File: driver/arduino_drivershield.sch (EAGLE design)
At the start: 13 parts, among them IC1 LB1973M, IC10 74HC14D, IC11 74HC14D, IC2 LB1973M, IC3 LB1973M, IC4 LB1973M, IC5 LB1973M, IC6 LB1973M, IC7 LB1973M, IC8 LB1973M, IC9 74HC14D, U1 ARDUINO_SHIELDLABEL

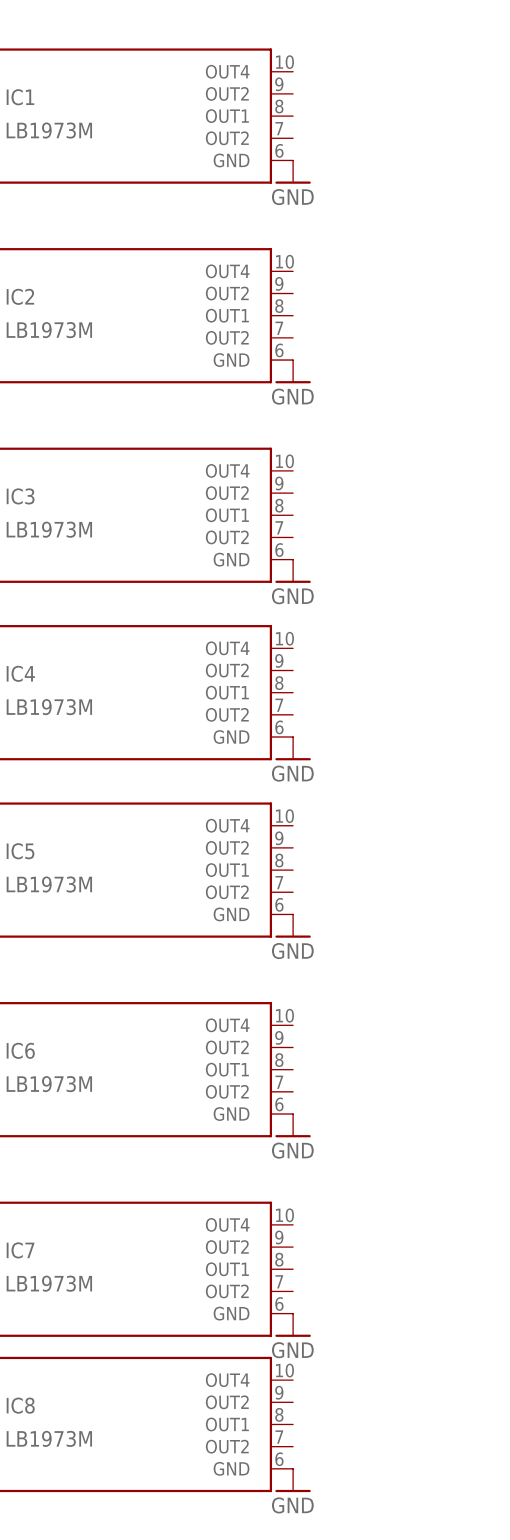
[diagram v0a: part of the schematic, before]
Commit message: 2x4 connectors for the coils
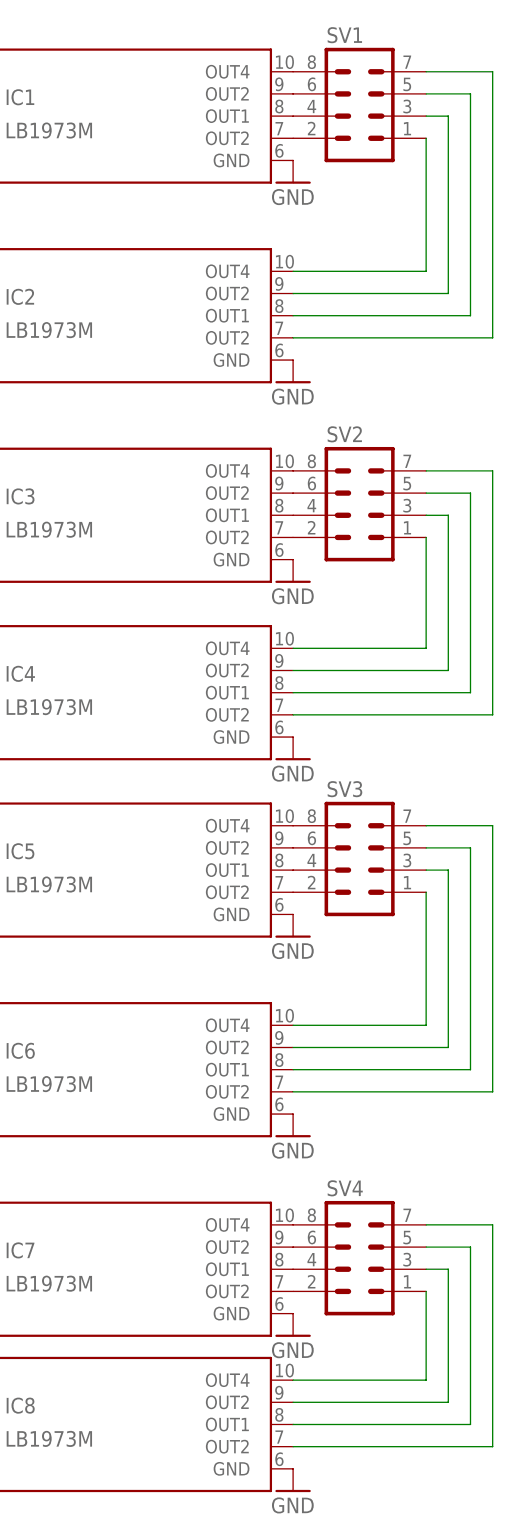
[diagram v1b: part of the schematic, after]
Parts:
- added SV1, SV2, SV3, SV4: (no value), con-lstb:MA04-2
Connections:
- new net N$33: IC1.OUT2, SV1.2
- new net N$34: IC1.OUT1, SV1.4
- new net N$35: IC1.OUT2@1, SV1.6
- new net N$36: IC1.OUT4, SV1.8
- new net N$37: IC3.OUT2, SV2.2
- new net N$38: IC3.OUT1, SV2.4
- new net N$39: IC3.OUT2@1, SV2.6
- new net N$40: IC3.OUT4, SV2.8
- new net N$41: IC5.OUT2, SV3.2
- new net N$42: IC5.OUT1, SV3.4
- new net N$43: IC5.OUT2@1, SV3.6
- new net N$44: IC5.OUT4, SV3.8
- new net N$45: IC7.OUT2, SV4.2
- new net N$46: IC7.OUT1, SV4.4
- new net N$47: IC7.OUT2@1, SV4.6
- new net N$48: IC7.OUT4, SV4.8
- new net N$49: IC8.OUT4, SV4.1
- new net N$50: IC8.OUT2@1, SV4.3
- new net N$51: IC8.OUT1, SV4.5
- new net N$52: IC8.OUT2, SV4.7
- new net N$53: IC6.OUT4, SV3.1
- new net N$54: IC6.OUT2@1, SV3.3
- new net N$55: IC6.OUT1, SV3.5
- new net N$56: IC6.OUT2, SV3.7
- new net N$57: IC4.OUT4, SV2.1
- new net N$58: IC4.OUT2@1, SV2.3
- new net N$59: IC4.OUT1, SV2.5
- new net N$60: IC4.OUT2, SV2.7
- new net N$61: IC2.OUT4, SV1.1
- new net N$62: IC2.OUT2@1, SV1.3
- new net N$63: IC2.OUT1, SV1.5
- new net N$64: IC2.OUT2, SV1.7

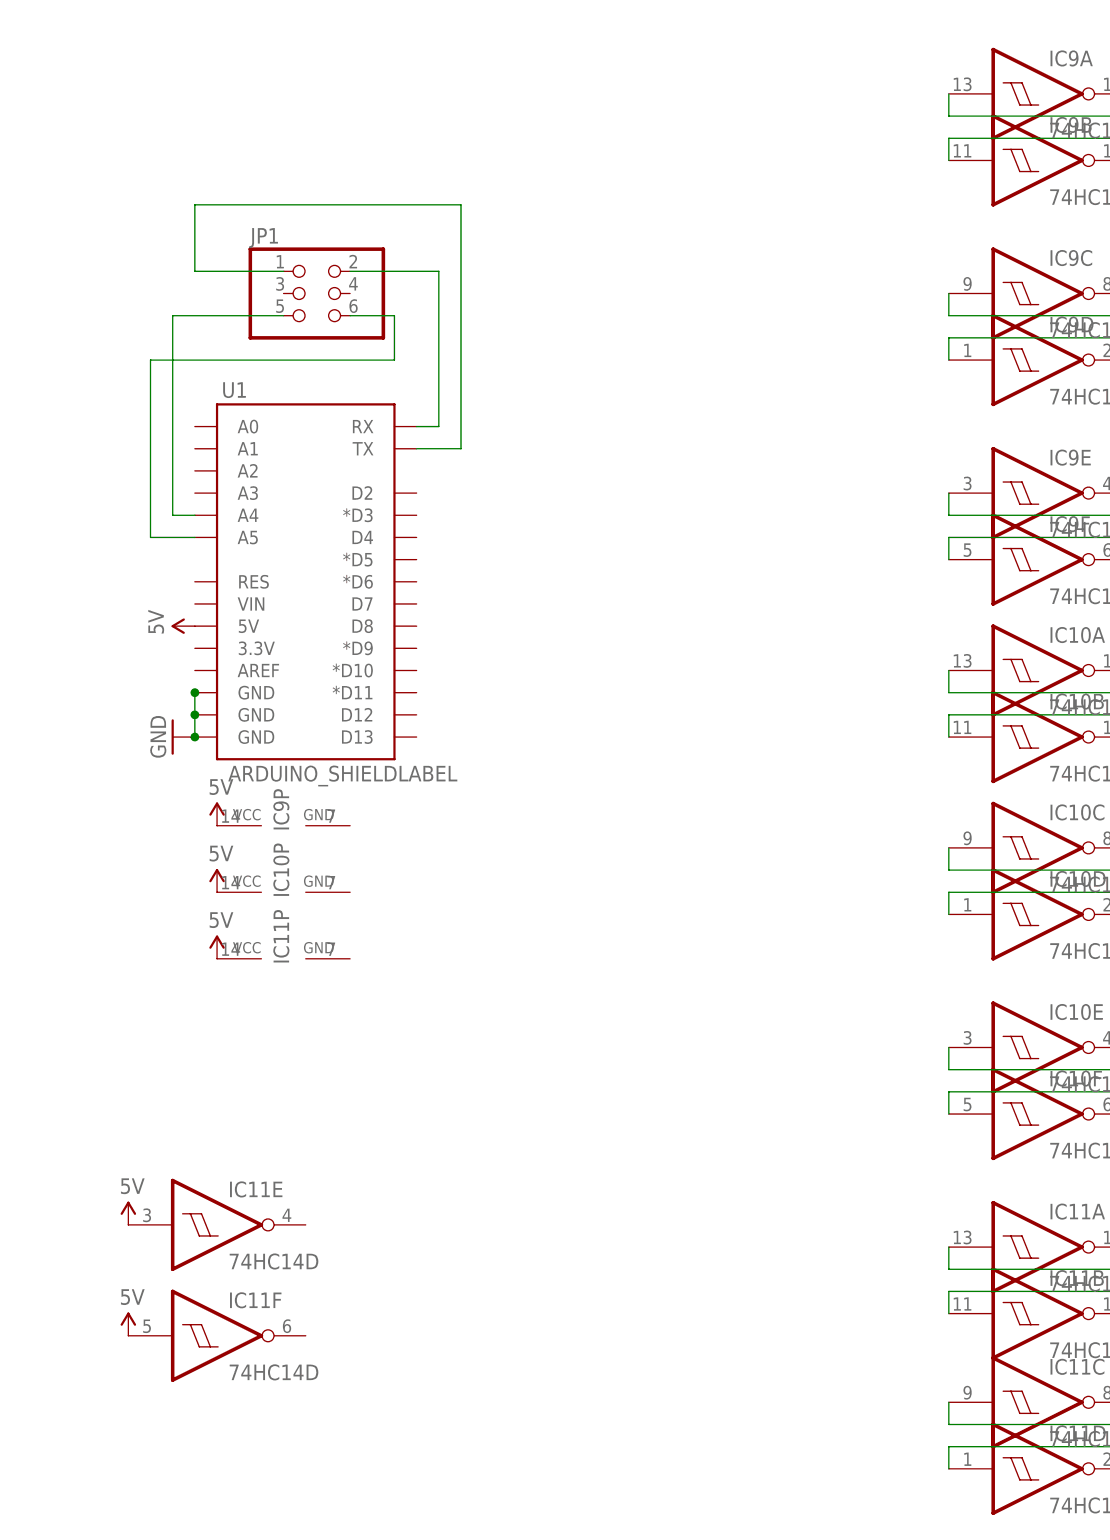
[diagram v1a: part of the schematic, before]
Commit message: wire the logic pins, this is all very initial the whole placement needs to be redone and some pins may need to be shuffled around
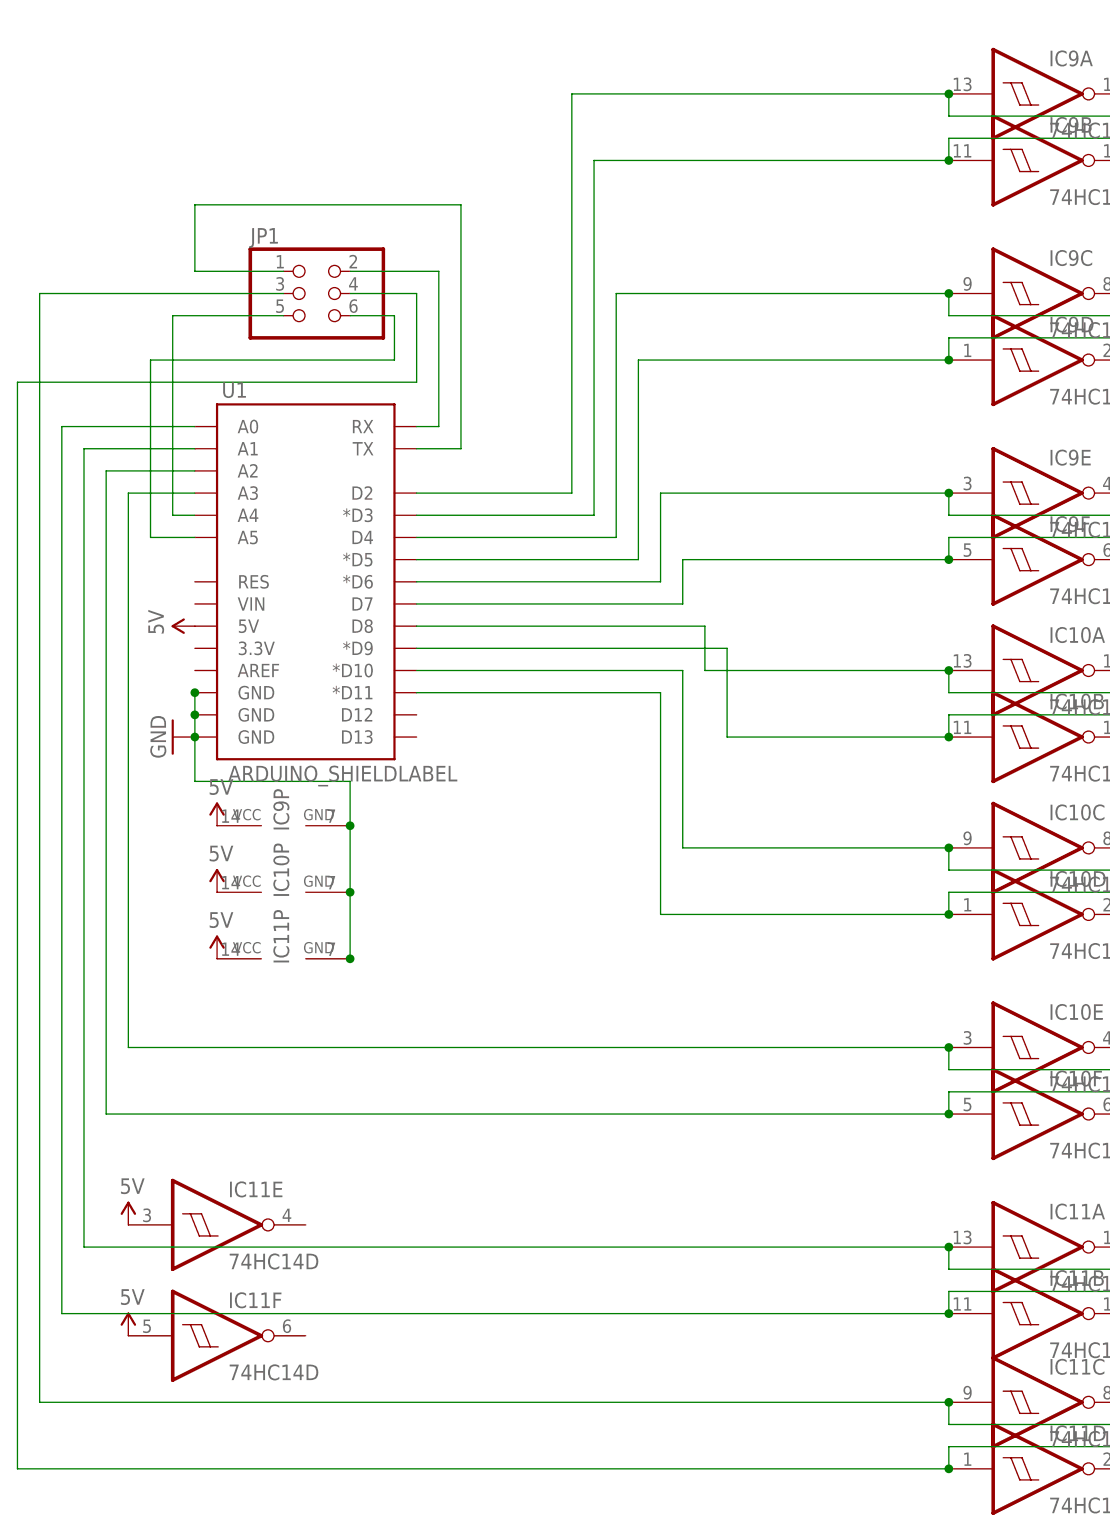
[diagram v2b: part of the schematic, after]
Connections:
- net GND: now also IC10P.GND, IC11P.GND, IC9P.GND
- net N$17: now also U1.D2
- net N$18: now also U1.*D3
- net N$19: now also U1.D4
- net N$20: now also U1.*D5
- net N$21: now also U1.*D6
- net N$22: now also U1.D7
- net N$23: now also U1.D8
- net N$24: now also U1.*D9
- net N$25: now also U1.*D10
- net N$26: now also U1.*D11
- net N$27: now also U1.A3
- net N$28: now also U1.A2
- net N$29: now also U1.A1
- net N$30: now also U1.A0
- net N$31: now also JP1.3
- net N$32: now also JP1.4
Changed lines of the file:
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@@
 <wire x1="12.7" y1="15.24" x2="12.7" y2="17.78" width="0.1524" layer="91"/>
 <junction x="12.7" y="17.78"/>
+<pinref part="IC9" gate="P" pin="GND"/>
+<pinref part="IC11" gate="P" pin="GND"/>
+<wire x1="30.48" y1="2.54" x2="30.48" y2="-5.08" width="0.1524" layer="91"/>
+<wire x1="30.48" y1="-5.08" x2="30.48" y2="-12.7" width="0.1524" layer="91"/>
+<wire x1="30.48" y1="2.54" x2="30.48" y2="7.62" width="0.1524" layer="91"/>
+<wire x1="30.48" y1="7.62" x2="12.7" y2="7.62" width="0.1524" layer="91"/>
+<wire x1="12.7" y1="7.62" x2="12.7" y2="12.7" width="0.1524" layer="91"/>
+<junction x="30.48" y="2.54"/>
+<pinref part="IC10" gate="P" pin="GND"/>
+<junction x="30.48" y="-5.08"/>
+<junction x="30.48" y="-12.7"/>
 </segment>
 <segment>
@@
 <wire x1="119.38" y1="83.82" x2="99.06" y2="83.82" width="0.1524" layer="91"/>
 <wire x1="99.06" y1="83.82" x2="99.06" y2="86.36" width="0.1524" layer="91"/>
+<pinref part="U1" gate="G$1" pin="D2"/>
+<wire x1="38.1" y1="40.64" x2="55.88" y2="40.64" width="0.1524" layer="91"/>
+<wire x1="55.88" y1="40.64" x2="55.88" y2="86.36" width="0.1524" layer="91"/>
+<wire x1="55.88" y1="86.36" x2="99.06" y2="86.36" width="0.1524" layer="91"/>
+<junction x="99.06" y="86.36"/>
 </segment>
 </net>
@@
 <wire x1="119.38" y1="81.28" x2="99.06" y2="81.28" width="0.1524" layer="91"/>
 <wire x1="99.06" y1="81.28" x2="99.06" y2="78.74" width="0.1524" layer="91"/>
+<wire x1="99.06" y1="78.74" x2="58.42" y2="78.74" width="0.1524" layer="91"/>
+<wire x1="58.42" y1="78.74" x2="58.42" y2="38.1" width="0.1524" layer="91"/>
+<pinref part="U1" gate="G$1" pin="*D3"/>
+<wire x1="58.42" y1="38.1" x2="38.1" y2="38.1" width="0.1524" layer="91"/>
+<junction x="99.06" y="78.74"/>
 </segment>
 </net>
@@
 <wire x1="119.38" y1="60.96" x2="99.06" y2="60.96" width="0.1524" layer="91"/>
 <wire x1="99.06" y1="60.96" x2="99.06" y2="63.5" width="0.1524" layer="91"/>
+<wire x1="99.06" y1="63.5" x2="60.96" y2="63.5" width="0.1524" layer="91"/>
+<wire x1="60.96" y1="63.5" x2="60.96" y2="35.56" width="0.1524" layer="91"/>
+<pinref part="U1" gate="G$1" pin="D4"/>
+<wire x1="60.96" y1="35.56" x2="38.1" y2="35.56" width="0.1524" layer="91"/>
+<junction x="99.06" y="63.5"/>
 </segment>
 </net>
@@
 <wire x1="119.38" y1="58.42" x2="99.06" y2="58.42" width="0.1524" layer="91"/>
 <wire x1="99.06" y1="58.42" x2="99.06" y2="55.88" width="0.1524" layer="91"/>
+<wire x1="99.06" y1="55.88" x2="63.5" y2="55.88" width="0.1524" layer="91"/>
+<wire x1="63.5" y1="55.88" x2="63.5" y2="33.02" width="0.1524" layer="91"/>
+<pinref part="U1" gate="G$1" pin="*D5"/>
+<wire x1="63.5" y1="33.02" x2="38.1" y2="33.02" width="0.1524" layer="91"/>
+<junction x="99.06" y="55.88"/>
 </segment>
 </net>
@@
 <wire x1="119.38" y1="38.1" x2="99.06" y2="38.1" width="0.1524" layer="91"/>
 <wire x1="99.06" y1="38.1" x2="99.06" y2="40.64" width="0.1524" layer="91"/>
+<wire x1="99.06" y1="40.64" x2="66.04" y2="40.64" width="0.1524" layer="91"/>
+<wire x1="66.04" y1="40.64" x2="66.04" y2="30.48" width="0.1524" layer="91"/>
+<pinref part="U1" gate="G$1" pin="*D6"/>
+<wire x1="66.04" y1="30.48" x2="38.1" y2="30.48" width="0.1524" layer="91"/>
+<junction x="99.06" y="40.64"/>
 </segment>
 </net>
@@
 <wire x1="119.38" y1="35.56" x2="99.06" y2="35.56" width="0.1524" layer="91"/>
 <wire x1="99.06" y1="35.56" x2="99.06" y2="33.02" width="0.1524" layer="91"/>
+<wire x1="99.06" y1="33.02" x2="68.58" y2="33.02" width="0.1524" layer="91"/>
+<wire x1="68.58" y1="33.02" x2="68.58" y2="27.94" width="0.1524" layer="91"/>
+<pinref part="U1" gate="G$1" pin="D7"/>
+<wire x1="68.58" y1="27.94" x2="38.1" y2="27.94" width="0.1524" layer="91"/>
+<junction x="99.06" y="33.02"/>
 </segment>
 </net>
@@
 <wire x1="119.38" y1="17.78" x2="99.06" y2="17.78" width="0.1524" layer="91"/>
 <wire x1="99.06" y1="17.78" x2="99.06" y2="20.32" width="0.1524" layer="91"/>
+<wire x1="99.06" y1="20.32" x2="71.12" y2="20.32" width="0.1524" layer="91"/>
+<wire x1="71.12" y1="20.32" x2="71.12" y2="25.4" width="0.1524" layer="91"/>
+<pinref part="U1" gate="G$1" pin="D8"/>
+<wire x1="71.12" y1="25.4" x2="38.1" y2="25.4" width="0.1524" layer="91"/>
+<junction x="99.06" y="20.32"/>
 </segment>
 </net>
@@
 <wire x1="119.38" y1="15.24" x2="99.06" y2="15.24" width="0.1524" layer="91"/>
 <wire x1="99.06" y1="15.24" x2="99.06" y2="12.7" width="0.1524" layer="91"/>
+<wire x1="99.06" y1="12.7" x2="73.66" y2="12.7" width="0.1524" layer="91"/>
+<wire x1="73.66" y1="12.7" x2="73.66" y2="22.86" width="0.1524" layer="91"/>
+<pinref part="U1" gate="G$1" pin="*D9"/>
+<wire x1="73.66" y1="22.86" x2="38.1" y2="22.86" width="0.1524" layer="91"/>
+<junction x="99.06" y="12.7"/>
 </segment>
 </net>
@@
 <wire x1="119.38" y1="-2.54" x2="99.06" y2="-2.54" width="0.1524" layer="91"/>
 <wire x1="99.06" y1="-2.54" x2="99.06" y2="0" width="0.1524" layer="91"/>
+<wire x1="99.06" y1="0" x2="68.58" y2="0" width="0.1524" layer="91"/>
+<wire x1="68.58" y1="0" x2="68.58" y2="20.32" width="0.1524" layer="91"/>
+<pinref part="U1" gate="G$1" pin="*D10"/>
+<wire x1="68.58" y1="20.32" x2="38.1" y2="20.32" width="0.1524" layer="91"/>
+<junction x="99.06" y="0"/>
 </segment>
 </net>
@@
 <wire x1="119.38" y1="-5.08" x2="99.06" y2="-5.08" width="0.1524" layer="91"/>
 <wire x1="99.06" y1="-5.08" x2="99.06" y2="-7.62" width="0.1524" layer="91"/>
+<wire x1="99.06" y1="-7.62" x2="66.04" y2="-7.62" width="0.1524" layer="91"/>
+<wire x1="66.04" y1="-7.62" x2="66.04" y2="17.78" width="0.1524" layer="91"/>
+<pinref part="U1" gate="G$1" pin="*D11"/>
+<wire x1="66.04" y1="17.78" x2="38.1" y2="17.78" width="0.1524" layer="91"/>
+<junction x="99.06" y="-7.62"/>
 </segment>
 </net>
@@
 <wire x1="119.38" y1="-25.4" x2="99.06" y2="-25.4" width="0.1524" layer="91"/>
 <wire x1="99.06" y1="-25.4" x2="99.06" y2="-22.86" width="0.1524" layer="91"/>
+<junction x="99.06" y="-22.86"/>
+<pinref part="U1" gate="G$1" pin="A3"/>
+<wire x1="12.7" y1="40.64" x2="5.08" y2="40.64" width="0.1524" layer="91"/>
+<wire x1="5.08" y1="40.64" x2="5.08" y2="-22.86" width="0.1524" layer="91"/>
+<wire x1="99.06" y1="-22.86" x2="5.08" y2="-22.86" width="0.1524" layer="91"/>
 </segment>
 </net>
@@
 <wire x1="119.38" y1="-27.94" x2="99.06" y2="-27.94" width="0.1524" layer="91"/>
 <wire x1="99.06" y1="-27.94" x2="99.06" y2="-30.48" width="0.1524" layer="91"/>
+<junction x="99.06" y="-30.48"/>
+<pinref part="U1" gate="G$1" pin="A2"/>
+<wire x1="12.7" y1="43.18" x2="2.54" y2="43.18" width="0.1524" layer="91"/>
+<wire x1="2.54" y1="43.18" x2="2.54" y2="-30.48" width="0.1524" layer="91"/>
+<wire x1="99.06" y1="-30.48" x2="2.54" y2="-30.48" width="0.1524" layer="91"/>
 </segment>
 </net>
@@
 <wire x1="119.38" y1="-48.26" x2="99.06" y2="-48.26" width="0.1524" layer="91"/>
 <wire x1="99.06" y1="-48.26" x2="99.06" y2="-45.72" width="0.1524" layer="91"/>
+<junction x="99.06" y="-45.72"/>
+<wire x1="99.06" y1="-45.72" x2="0" y2="-45.72" width="0.1524" layer="91"/>
+<pinref part="U1" gate="G$1" pin="A1"/>
+<wire x1="12.7" y1="45.72" x2="0" y2="45.72" width="0.1524" layer="91"/>
+<wire x1="0" y1="45.72" x2="0" y2="-45.72" width="0.1524" layer="91"/>
 </segment>
 </net>
@@
 <wire x1="119.38" y1="-50.8" x2="99.06" y2="-50.8" width="0.1524" layer="91"/>
 <wire x1="99.06" y1="-50.8" x2="99.06" y2="-53.34" width="0.1524" layer="91"/>
+<junction x="99.06" y="-53.34"/>
+<pinref part="U1" gate="G$1" pin="A0"/>
+<wire x1="12.7" y1="48.26" x2="-2.54" y2="48.26" width="0.1524" layer="91"/>
+<wire x1="-2.54" y1="48.26" x2="-2.54" y2="-53.34" width="0.1524" layer="91"/>
+<wire x1="99.06" y1="-53.34" x2="-2.54" y2="-53.34" width="0.1524" layer="91"/>
 </segment>
 </net>
@@
 <wire x1="119.38" y1="-66.04" x2="99.06" y2="-66.04" width="0.1524" layer="91"/>
 <wire x1="99.06" y1="-66.04" x2="99.06" y2="-63.5" width="0.1524" layer="91"/>
+<junction x="99.06" y="-63.5"/>
+<pinref part="JP1" gate="A" pin="3"/>
+<wire x1="22.86" y1="63.5" x2="-5.08" y2="63.5" width="0.1524" layer="91"/>
+<wire x1="-5.08" y1="63.5" x2="-5.08" y2="-63.5" width="0.1524" layer="91"/>
+<wire x1="99.06" y1="-63.5" x2="-5.08" y2="-63.5" width="0.1524" layer="91"/>
 </segment>
 </net>
@@
 <wire x1="119.38" y1="-68.58" x2="99.06" y2="-68.58" width="0.1524" layer="91"/>
 <wire x1="99.06" y1="-68.58" x2="99.06" y2="-71.12" width="0.1524" layer="91"/>
+<junction x="99.06" y="-71.12"/>
+<pinref part="JP1" gate="A" pin="4"/>
+<wire x1="30.48" y1="63.5" x2="38.1" y2="63.5" width="0.1524" layer="91"/>
+<wire x1="38.1" y1="63.5" x2="38.1" y2="53.34" width="0.1524" layer="91"/>
+<wire x1="38.1" y1="53.34" x2="-7.62" y2="53.34" width="0.1524" layer="91"/>
+<wire x1="-7.62" y1="53.34" x2="-7.62" y2="-71.12" width="0.1524" layer="91"/>
+<wire x1="99.06" y1="-71.12" x2="-7.62" y2="-71.12" width="0.1524" layer="91"/>
 </segment>
 </net>
@@
 </sheet>
 </sheets>
+<errors>
+</errors>
 </schematic>
 </drawing>
